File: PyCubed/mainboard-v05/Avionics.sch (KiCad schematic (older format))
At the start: 41 parts, among them J10 Conn_01x04, J15 Conn_01x02, J8 Conn_01x09, J9 Conn_01x03, SW1 KMR231NG LFS, U1 MAX706RESA, U2 ATSAMD51J19A-AU, U3 BMX160, Y1 32.768kHz

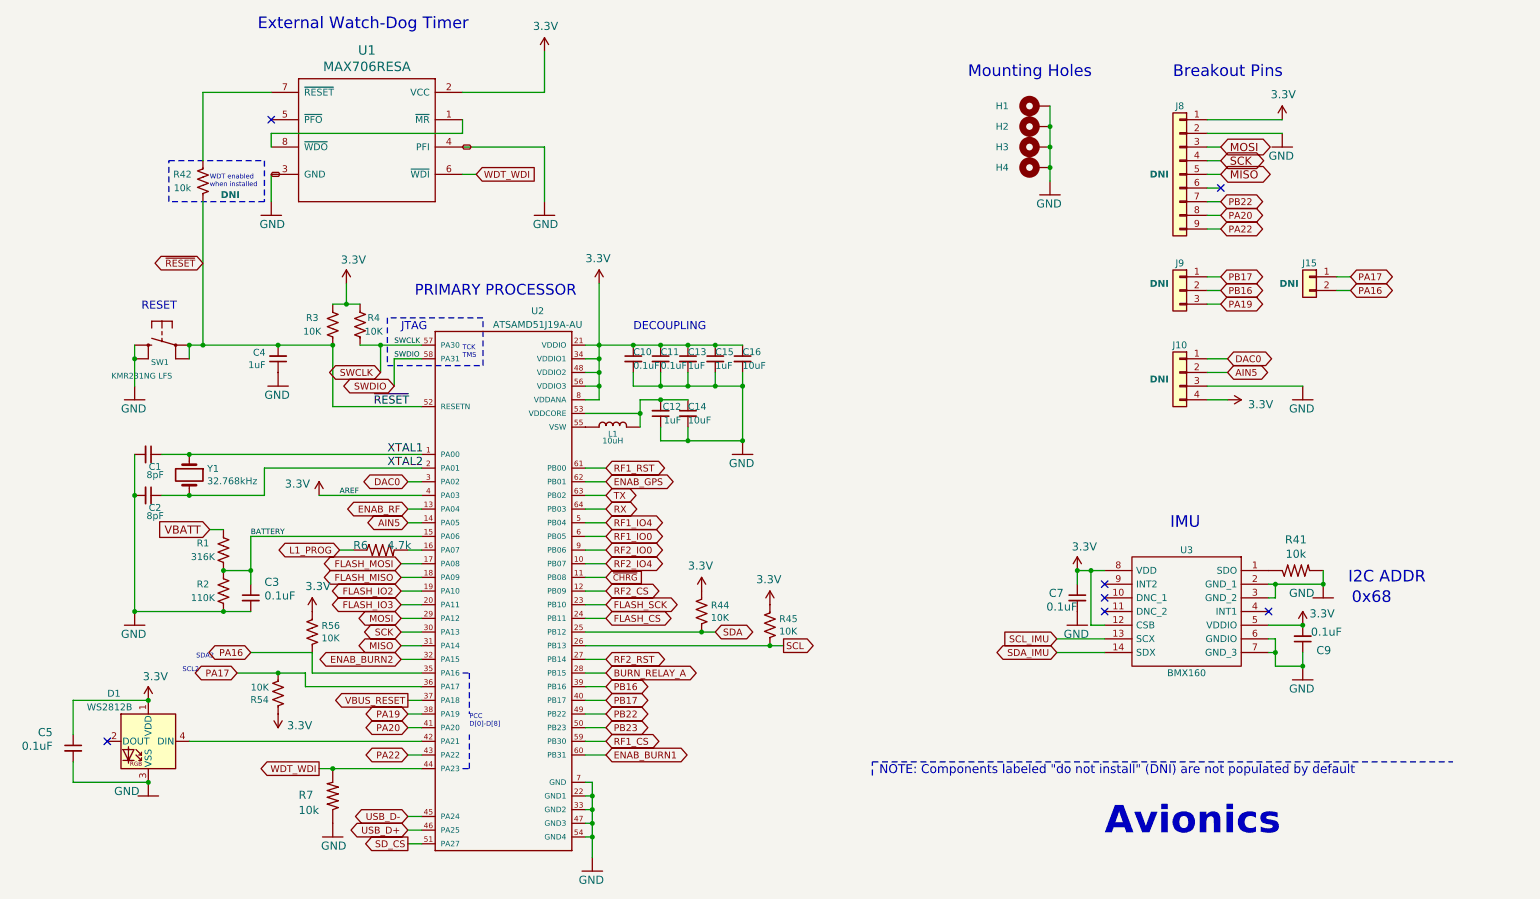
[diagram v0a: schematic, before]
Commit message: Battery board and side panels ready for CAD check and review, pycubed not finished yet
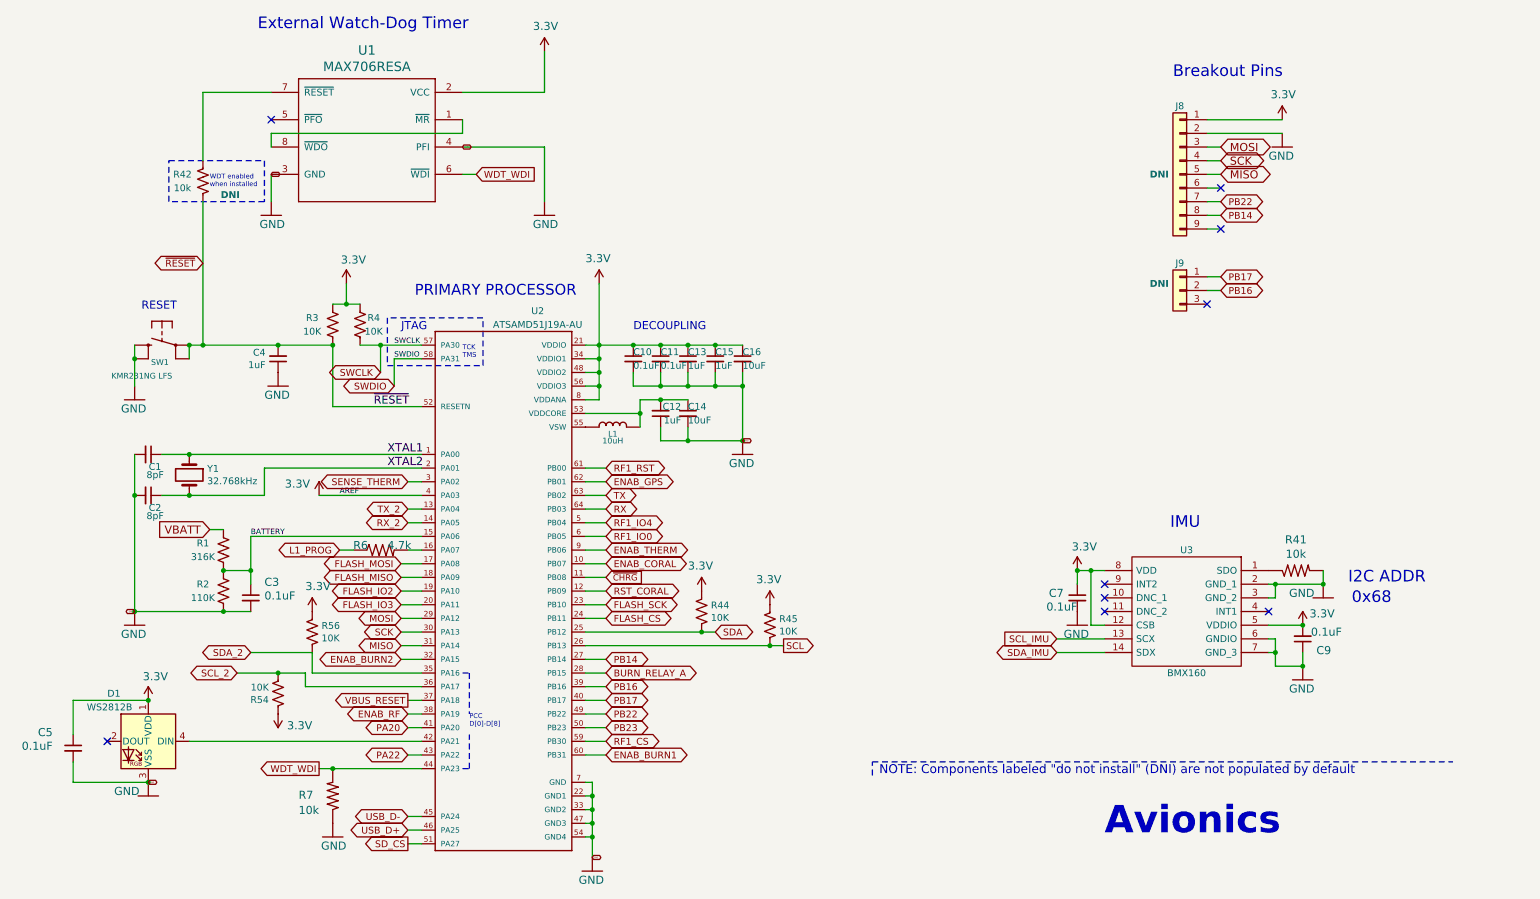
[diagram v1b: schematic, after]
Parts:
- removed H1, H2, H3, H4: MountingHole_Pad, MountingHole:MountingHole_3.2mm_M3_DIN965_Pad, symbol Mechanical:MountingHole_Pad
- removed J10: Conn_01x04, Connector_PinHeader_2.54mm:PinHeader_1x04_P2.54mm_Vertical, symbol Connector_Generic:Conn_01x04
- removed J15: Conn_01x02, mainboard:PinHeader_CUSTOM3, symbol Connector_Generic:Conn_01x02
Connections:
- net ENAB_RF: now also U2.38 (PA19); no longer U2.13 (PA04)
- net GND: now also C1.2, C10.2, C11.2, C12.1, C13.2, C14.2, C15.2, C16.2, C2.2, C3.2, C5.2, D1.3 (VSS), R2.1, U2.22 (GND1), U2.33 (GND2), U2.47 (GND3), U2.54 (GND4), U2.7 (GND)
- net PA20: no longer J8.8 (Pin_8)
- net PA22: no longer J8.9 (Pin_9)
- net AIN5 renamed RX_2
- net DAC0 renamed SENSE_THERM
- net PA16 renamed SDA_2
- net PA17 renamed SCL_2
- net PA19: no longer names the net of J9.3 (Pin_3)
- net PA19: no longer U2.38 (PA19)
- net RF2_CS renamed RST_CORAL
- net RF2_IO0 renamed ENAB_THERM
- net RF2_IO4 renamed ENAB_CORAL
- net RF2_RST renamed PB14
- net PB14: now also J8.8 (Pin_8)
- new net TX_2: U2.13 (PA04)
- no-connect marks 7 -> 9
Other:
- note removed: "Mounting Holes"
- note removed: "SCL2"
- note removed: "SDA2"
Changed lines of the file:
@@
-$EndComp
-$Comp
-L mainboard:MAX708RESA-T U1
-U 1 1 5D6DE815
-P 4050 1600
-F 0 "U1" H 4850 2008 69  0000 C CNN
-F 1 "MAX706RESA" H 4850 1888 69  0000 C CNN
-F 2 "Package_SO:SO-8_3.9x4.9mm_P1.27mm" H 4050 1600 50  0001 C CNN
-F 3 "https://datasheets.maximintegrated.com/en/ds/MAX706AP-MAX708T.pdf" H 4050 1600 50  0001 C CNN
-F 4 "Watch-dog Timer" H 4050 1600 50  0001 C CNN "Description"
-F 5 "MAX706RESA" H 4050 1600 50  0001 C CNN "Flight"
-F 6 "Maxim Integrated" H 4050 1600 50  0001 C CNN "Manufacturer_Name"
-F 7 "MAX706RESA" H 4850 2108 50  0001 C CNN "Manufacturer_Part_Number"
-F 8 "MAX706RESA" H 4050 1600 50  0001 C CNN "Proto"
-	1    4050 1600
-	-1   0    0    -1
 $EndComp
 $Comp
@@
 $EndComp
 $Comp
-L Mechanical:MountingHole_Pad H1
-U 1 1 5D4B48C8
-P 8150 1600
-F 0 "H1" V 8150 1850 50  0000 C CNN
-F 1 "MountingHole_Pad" V 8296 1603 50  0001 C CNN
-F 2 "MountingHole:MountingHole_3.2mm_M3_DIN965_Pad" H 8150 1600 50  0001 C CNN
-F 3 "" H 8150 1600 50  0001 C CNN
-F 4 "DNI" H 8150 1600 50  0001 C CNN "DNI"
-	1    8150 1600
-	0    -1   -1   0
-$EndComp
-$Comp
-L mainboard:GND #GND?
-U 1 1 5D4B6248
-P 8250 2250
-AR Path="/5D4B6248" Ref="#GND?"  Part="1"
-AR Path="/5CEC5A72/5D4B6248" Ref="#GND0102"  Part="1"
-F 0 "#GND0102" H 8250 2250 50  0001 C CNN
-F 1 "GND" H 8150 2150 59  0000 L BNN
-F 2 "" H 8250 2250 50  0001 C CNN
-F 3 "" H 8250 2250 50  0001 C CNN
-	1    8250 2250
-	1    0    0    -1
-$EndComp
-$Comp
-L Mechanical:MountingHole_Pad H2
-U 1 1 5D4D6590
-P 8150 1750
-F 0 "H2" V 8150 2000 50  0000 C CNN
-F 1 "MountingHole_Pad" V 8296 1753 50  0001 C CNN
-F 2 "MountingHole:MountingHole_3.2mm_M3_DIN965_Pad" H 8150 1750 50  0001 C CNN
-F 3 "" H 8150 1750 50  0001 C CNN
-F 4 "DNI" H 8150 1750 50  0001 C CNN "DNI"
-	1    8150 1750
-	0    -1   -1   0
-$EndComp
-$Comp
-L Mechanical:MountingHole_Pad H3
-U 1 1 5D4D66B4
-P 8150 1900
-F 0 "H3" V 8150 2150 50  0000 C CNN
-F 1 "MountingHole_Pad" V 8296 1903 50  0001 C CNN
-F 2 "MountingHole:MountingHole_3.2mm_M3_DIN965_Pad" H 8150 1900 50  0001 C CNN
-F 3 "" H 8150 1900 50  0001 C CNN
-F 4 "DNI" H 8150 1900 50  0001 C CNN "DNI"
-	1    8150 1900
-	0    -1   -1   0
-$EndComp
-$Comp
-L Mechanical:MountingHole_Pad H4
-U 1 1 5D4D67E3
-P 8150 2050
-F 0 "H4" V 8150 2300 50  0000 C CNN
-F 1 "MountingHole_Pad" V 8296 2053 50  0001 C CNN
-F 2 "MountingHole:MountingHole_3.2mm_M3_DIN965_Pad" H 8150 2050 50  0001 C CNN
-F 3 "" H 8150 2050 50  0001 C CNN
-F 4 "DNI" H 8150 2050 50  0001 C CNN "DNI"
-	1    8150 2050
-	0    -1   -1   0
-$EndComp
-$Comp
 L Device:R_US R42
 U 1 1 5D3DC34B
@@
 	1    2050 2150
 	1    0    0    1
-$EndComp
-$Comp
-L mainboard:3.3V #SUPPLY?
-U 1 1 5DE0EDF6
-P 9550 3750
-AR Path="/5DE0EDF6" Ref="#SUPPLY?"  Part="1"
-AR Path="/5CEC5A72/5DE0EDF6" Ref="#SUPPLY0115"  Part="1"
-F 0 "#SUPPLY0115" H 9550 3750 50  0001 C CNN
-F 1 "3.3V" V 9550 3900 59  0000 L BNN
-F 2 "" H 9550 3750 50  0001 C CNN
-F 3 "" H 9550 3750 50  0001 C CNN
-	1    9550 3750
-	0    1    -1   0
-$EndComp
-$Comp
-L mainboard:GND #GND?
-U 1 1 5DE0EDFC
-P 10100 3750
-AR Path="/5DE0EDFC" Ref="#GND?"  Part="1"
-AR Path="/5CEC5A72/5DE0EDFC" Ref="#GND0111"  Part="1"
-F 0 "#GND0111" H 10100 3750 50  0001 C CNN
-F 1 "GND" H 10000 3650 59  0000 L BNN
-F 2 "" H 10100 3750 50  0001 C CNN
-F 3 "" H 10100 3750 50  0001 C CNN
-	1    10100 3750
-	1    0    0    -1
 $EndComp
 $Comp
@@
 	-1   0    0    -1
 $EndComp
-$Comp
-L Connector_Generic:Conn_01x02 J15
-U 1 1 5EE1CFC2
-P 10150 2850
-F 0 "J15" H 10150 2950 50  0000 C CNN
-F 1 "Conn_01x02" H 10068 2976 50  0001 C CNN
-F 2 "mainboard:PinHeader_CUSTOM3" H 10150 2850 50  0001 C CNN
-F 3 "" H 10150 2850 50  0001 C CNN
-F 4 "DNI" H 10300 2800 50  0000 C CNB "DNI"
-F 5 "2-pin Vertical Header - 0.1in (2.54mm)" H 10150 2850 50  0001 C CNN "Description"
-	1    10150 2850
-	-1   0    0    -1
-$EndComp
-$Comp
-L Connector_Generic:Conn_01x04 J10
-U 1 1 60A5E520
-P 9200 3550
-F 0 "J10" H 9200 3750 50  0000 C CNN
-F 1 "Conn_01x04" H 9118 3866 50  0001 C CNN
-F 2 "Connector_PinHeader_2.54mm:PinHeader_1x04_P2.54mm_Vertical" H 9200 3550 50  0001 C CNN
-F 3 "" H 9200 3550 50  0001 C CNN
-F 4 "DNI" H 9350 3500 50  0000 C CNB "DNI"
-F 5 "Vertical Header - 0.1in (2.54mm)" H 9200 3550 50  0001 C CNN "Description"
-	1    9200 3550
-	-1   0    0    -1
-$EndComp
 Text GLabel 2550 2100 2    10   BiDi ~ 0
-GND
-Text GLabel 3950 1900 2    10   BiDi ~ 0
 GND
 Text GLabel 5000 4450 2    50   BiDi ~ 0
@@
 PA22
 Text GLabel 3550 6050 0    50   BiDi ~ 0
-PA19
+ENAB_RF
 Text GLabel 9500 1900 2    59   BiDi ~ 0
 MOSI
@@
 Text GLabel 4050 2100 2    50   Input ~ 0
 WDT_WDI
-Text GLabel 9500 2400 2    50   BiDi ~ 0
-PA20
-Text GLabel 9500 2500 2    50   BiDi ~ 0
-PA22
 Text GLabel 9500 2300 2    50   BiDi ~ 0
 PB22
 Text GLabel 3550 4350 0    50   BiDi ~ 0
-DAC0
+SENSE_THERM
 Text GLabel 5000 5850 2    50   BiDi ~ 0
 PB16
@@
 Text Notes 9150 1400 0    85   ~ 0
 Breakout Pins
-Text Notes 7650 1400 0    85   ~ 0
-Mounting Holes
 Text Notes 8650 6950 0    200  ~ 40
 Avionics
@@
 AREF
 Text GLabel 5000 4950 2    50   BiDi ~ 0
-RF2_IO4
+ENAB_CORAL
 Text GLabel 5000 5150 2    50   BiDi ~ 0
-RF2_CS
+RST_CORAL
 Text GLabel 5000 5650 2    50   BiDi ~ 0
-RF2_RST
-Text GLabel 9550 3450 2    50   BiDi ~ 0
-DAC0
+PB14
 Text GLabel 6300 5550 2    50   Output ~ 0
 SCL
@@
 RF1_IO4
 Text GLabel 5000 4850 2    50   BiDi ~ 0
-RF2_IO0
-Text GLabel 3550 4550 0    50   BiDi ~ 0
-ENAB_RF
+ENAB_THERM
 Text GLabel 3550 4650 0    50   BiDi ~ 0
-AIN5
-Text GLabel 9550 3550 2    50   BiDi ~ 0
-AIN5
+RX_2
 Text Notes 11000 5100 2    85   ~ 0
 I2C ADDR
@@
 Text GLabel 3550 5950 0    50   Output ~ 0
 VBUS_RESET
-Text GLabel 9500 3050 2    50   BiDi ~ 0
-PA19
 Text GLabel 9500 2950 2    50   BiDi ~ 0
 PB16
@@
 PB17
 Text GLabel 2400 5600 0    50   BiDi ~ 0
-PA16
-Text GLabel 10450 2850 2    50   BiDi ~ 0
-PA17
-Text GLabel 10450 2950 2    50   BiDi ~ 0
-PA16
+SDA_2
 Text GLabel 5000 4750 2    50   BiDi ~ 0
 RF1_IO0
 Wire Wire Line
-	2550 2100 2550 2300
-Wire Wire Line
-	3950 1900 4550 1900
-Wire Wire Line
-	4550 1900 4550 2300
-Wire Wire Line
 	4850 4450 5000 4450
 Wire Wire Line
@@
 	9400 2500 9500 2500
 Wire Wire Line
-	9400 2200 9500 2200
-Wire Wire Line
 	9400 2300 9500 2300
 Wire Wire Line
@@
 	3650 4350 3550 4350
 Wire Wire Line
-	8250 1600 8250 1750
-Wire Wire Line
-	8250 1750 8250 1900
-Wire Wire Line
-	8250 1900 8250 2050
-Wire Wire Line
-	8250 2050 8250 2150
-Wire Wire Line
 	3450 3450 3650 3450
 Wire Wire Line
@@
 	4850 5650 5000 5650
 Wire Wire Line
-	9550 3450 9400 3450
-Wire Wire Line
 	4850 4650 5000 4650
 Wire Wire Line
@@
 	3650 4650 3550 4650
 Wire Wire Line
-	9550 3550 9400 3550
-Wire Wire Line
 	2400 4750 3650 4750
 Wire Wire Line
-	9400 3650 10100 3650
-Wire Wire Line
-	9550 3750 9400 3750
-Wire Wire Line
 	10100 5400 9850 5400
 Wire Wire Line
@@
 	3550 5950 3650 5950
 Wire Wire Line
-	9400 3050 9500 3050
-Wire Wire Line
 	9400 2950 9500 2950
 Wire Wire Line
 	9400 2850 9500 2850
 Wire Wire Line
-	10450 2850 10350 2850
-Wire Wire Line
-	10450 2950 10350 2950
-Wire Wire Line
 	2050 1500 2050 2000
 Wire Wire Line
@@
 Wire Wire Line
 	2550 1800 3950 1800
-Wire Wire Line
-	3950 1800 3950 1700
 Connection ~ 4950 3350
 Connection ~ 4950 3450
@@
 Connection ~ 2200 5000
 Connection ~ 3000 6450
-Connection ~ 8250 1750
-Connection ~ 8250 1900
-Connection ~ 8250 2050
 Connection ~ 10100 5700
 Connection ~ 9900 5600
@@
 Wire Notes Line
 	4000 6450 4000 6200
-Text Notes 2000 5650 0    35   ~ 0
-SDA2
 Wire Wire Line
 	1950 6250 3650 6250
@@
 Connection ~ 1650 6550
 Connection ~ 1650 5950
-Text Notes 1900 5750 0    35   ~ 0
-SCL2
 Text GLabel 2300 5750 0    50   BiDi ~ 0
-PA17
+SCL_2
 $Comp
 L LED:WS2812B D1
@@
 	-1   0    0    -1
 $EndComp
+Text GLabel 3550 4550 0    50   BiDi ~ 0
+TX_2
+NoConn ~ 9400 3050
+NoConn ~ 9500 2500
+Wire Wire Line
+	9400 2200 9500 2200
+Text GLabel 9500 2400 2    50   BiDi ~ 0
+PB14
+Wire Wire Line
+	4550 1900 4550 2300
+Wire Wire Line
+	3950 1800 3950 1700
+Wire Wire Line
+	2550 2100 2550 2300
+Wire Wire Line
+	3950 1900 4550 1900
+$Comp
+L mainboard:MAX708RESA-T U1
+U 1 1 5D6DE815
+P 4050 1600
+F 0 "U1" H 4850 2008 69  0000 C CNN
+F 1 "MAX706RESA" H 4850 1888 69  0000 C CNN
+F 2 "Package_SO:SO-8_3.9x4.9mm_P1.27mm" H 4050 1600 50  0001 C CNN
+F 3 "https://datasheets.maximintegrated.com/en/ds/MAX706AP-MAX708T.pdf" H 4050 1600 50  0001 C CNN
+F 4 "Watch-dog Timer" H 4050 1600 50  0001 C CNN "Description"
+F 5 "MAX706RESA" H 4050 1600 50  0001 C CNN "Flight"
+F 6 "Maxim Integrated" H 4050 1600 50  0001 C CNN "Manufacturer_Name"
+F 7 "MAX706RESA" H 4850 2108 50  0001 C CNN "Manufacturer_Part_Number"
+F 8 "MAX706RESA" H 4050 1600 50  0001 C CNN "Proto"
+	1    4050 1600
+	-1   0    0    -1
+$EndComp
+Text GLabel 3950 1900 2    10   BiDi ~ 0
+GND
+Text GLabel 1550 5300 0    10   BiDi ~ 0
+GND
+Text GLabel 1650 6550 2    10   BiDi ~ 0
+GND
+Text GLabel 4900 7100 2    10   BiDi ~ 0
+GND
+Text GLabel 6000 4050 2    10   BiDi ~ 0
+GND
 NoConn ~ 9500 2200
 $EndSCHEMATC

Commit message: radio and gps moved to make space for limit switches
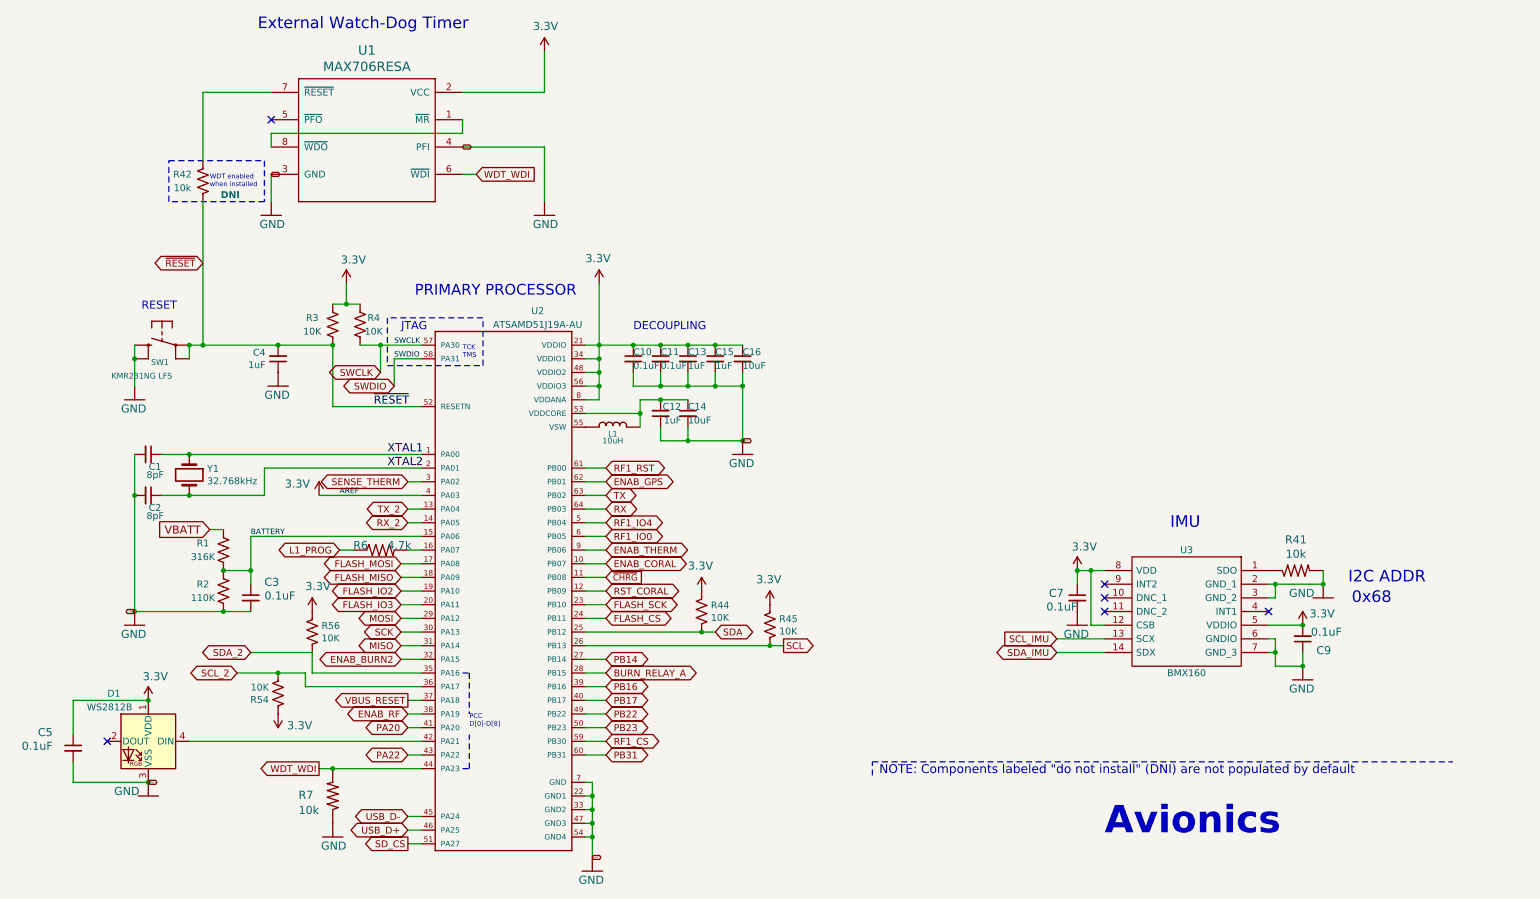
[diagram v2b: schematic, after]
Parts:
- removed J8: Conn_01x09, Connector_PinHeader_2.54mm:PinHeader_1x09_P2.54mm_Vertical, symbol Connector_Generic:Conn_01x09
- removed J9: Conn_01x03, Connector_PinHeader_2.54mm:PinHeader_1x03_P2.54mm_Vertical, symbol Connector_Generic:Conn_01x03
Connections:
- net ENAB_BURN1 renamed PB31
- no-connect marks 9 -> 6
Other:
- note removed: "Breakout Pins"
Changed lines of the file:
@@
-$EndComp
-$Comp
-L Connector_Generic:Conn_01x09 J8
-U 1 1 5D3643AA
-P 9200 2100
-F 0 "J8" H 9200 2600 50  0000 C CNN
-F 1 "Conn_01x09" H 9118 2626 50  0001 C CNN
-F 2 "Connector_PinHeader_2.54mm:PinHeader_1x09_P2.54mm_Vertical" H 9200 2100 50  0001 C CNN
-F 3 "" H 9200 2100 50  0001 C CNN
-F 4 "DNI" H 9350 2100 50  0000 C CNB "DNI"
-F 5 "Vertical Header - 0.1in (2.54mm)" H 9200 2100 50  0001 C CNN "Description"
-	1    9200 2100
-	-1   0    0    -1
-$EndComp
-$Comp
-L mainboard:3.3V #SUPPLY?
-U 1 1 5D370A56
-P 9950 1700
-AR Path="/5D370A56" Ref="#SUPPLY?"  Part="1"
-AR Path="/5CEC5A72/5D370A56" Ref="#SUPPLY0111"  Part="1"
-F 0 "#SUPPLY0111" H 9950 1700 50  0001 C CNN
-F 1 "3.3V" H 9850 1850 59  0000 L BNN
-F 2 "" H 9950 1700 50  0001 C CNN
-F 3 "" H 9950 1700 50  0001 C CNN
-	1    9950 1700
-	-1   0    0    -1
-$EndComp
-$Comp
-L mainboard:GND #GND?
-U 1 1 5D3722F9
-P 9950 1900
-AR Path="/5D3722F9" Ref="#GND?"  Part="1"
-AR Path="/5CEC5A72/5D3722F9" Ref="#GND0101"  Part="1"
-F 0 "#GND0101" H 9950 1900 50  0001 C CNN
-F 1 "GND" H 9850 1800 59  0000 L BNN
-F 2 "" H 9950 1900 50  0001 C CNN
-F 3 "" H 9950 1900 50  0001 C CNN
-	1    9950 1900
-	1    0    0    -1
 $EndComp
 $Comp
@@
 	1    0    0    -1
 $EndComp
-$Comp
-L Connector_Generic:Conn_01x03 J9
-U 1 1 5FC0A60F
-P 9200 2950
-F 0 "J9" H 9200 3150 50  0000 C CNN
-F 1 "Conn_01x03" H 9118 2626 50  0001 C CNN
-F 2 "Connector_PinHeader_2.54mm:PinHeader_1x03_P2.54mm_Vertical" H 9200 2950 50  0001 C CNN
-F 3 "" H 9200 2950 50  0001 C CNN
-F 4 "DNI" H 9350 3000 50  0000 C CNB "DNI"
-F 5 "Vertical Header - 0.1in (2.54mm)" H 9200 2950 50  0001 C CNN "Description"
-	1    9200 2950
-	-1   0    0    -1
-$EndComp
 Text GLabel 2550 2100 2    10   BiDi ~ 0
 GND
@@
 ENAB_BURN2
 Text GLabel 5000 6350 2    50   BiDi ~ 0
-ENAB_BURN1
+PB31
 Text GLabel 5000 5750 2    50   BiDi ~ 0
 BURN_RELAY_A
@@
 Text GLabel 3550 6050 0    50   BiDi ~ 0
 ENAB_RF
-Text GLabel 9500 1900 2    59   BiDi ~ 0
-MOSI
-Text GLabel 9500 2000 2    59   BiDi ~ 0
-SCK
-Text GLabel 9500 2100 2    59   BiDi ~ 0
-MISO
 Text GLabel 5000 5050 2    45   Input ~ 0
 ~CHRG
 Text GLabel 4050 2100 2    50   Input ~ 0
 WDT_WDI
-Text GLabel 9500 2300 2    50   BiDi ~ 0
-PB22
 Text GLabel 3550 4350 0    50   BiDi ~ 0
 SENSE_THERM
@@
 Text GLabel 5000 4250 2    50   BiDi ~ 0
 RF1_RST
-Text Notes 9150 1400 0    85   ~ 0
-Breakout Pins
 Text Notes 8650 6950 0    200  ~ 40
 Avionics
@@
 Text GLabel 3550 5950 0    50   Output ~ 0
 VBUS_RESET
-Text GLabel 9500 2950 2    50   BiDi ~ 0
-PB16
-Text GLabel 9500 2850 2    50   BiDi ~ 0
-PB17
 Text GLabel 2400 5600 0    50   BiDi ~ 0
 SDA_2
@@
 	3650 6050 3550 6050
 Wire Wire Line
-	9500 2000 9400 2000
-Wire Wire Line
-	9500 1900 9400 1900
-Wire Wire Line
-	9500 2100 9400 2100
-Wire Wire Line
 	5000 5050 4850 5050
 Wire Wire Line
@@
 	4850 5550 6200 5550
 Wire Wire Line
-	9400 2400 9500 2400
-Wire Wire Line
-	9400 2500 9500 2500
-Wire Wire Line
-	9400 2300 9500 2300
-Wire Wire Line
-	9400 1800 9950 1800
-Wire Wire Line
-	9950 1700 9400 1700
-Wire Wire Line
 	3650 4350 3550 4350
 Wire Wire Line
@@
 Wire Wire Line
 	3550 5950 3650 5950
-Wire Wire Line
-	9400 2950 9500 2950
-Wire Wire Line
-	9400 2850 9500 2850
 Wire Wire Line
 	2050 1500 2050 2000
@@
 Text GLabel 3550 4550 0    50   BiDi ~ 0
 TX_2
-NoConn ~ 9400 3050
-NoConn ~ 9500 2500
-Wire Wire Line
-	9400 2200 9500 2200
-Text GLabel 9500 2400 2    50   BiDi ~ 0
-PB14
 Wire Wire Line
 	4550 1900 4550 2300
@@
 Text GLabel 6000 4050 2    10   BiDi ~ 0
 GND
-NoConn ~ 9500 2200
 $EndSCHEMATC
